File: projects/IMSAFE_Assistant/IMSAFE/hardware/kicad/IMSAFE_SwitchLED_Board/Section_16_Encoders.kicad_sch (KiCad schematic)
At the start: 0 parts

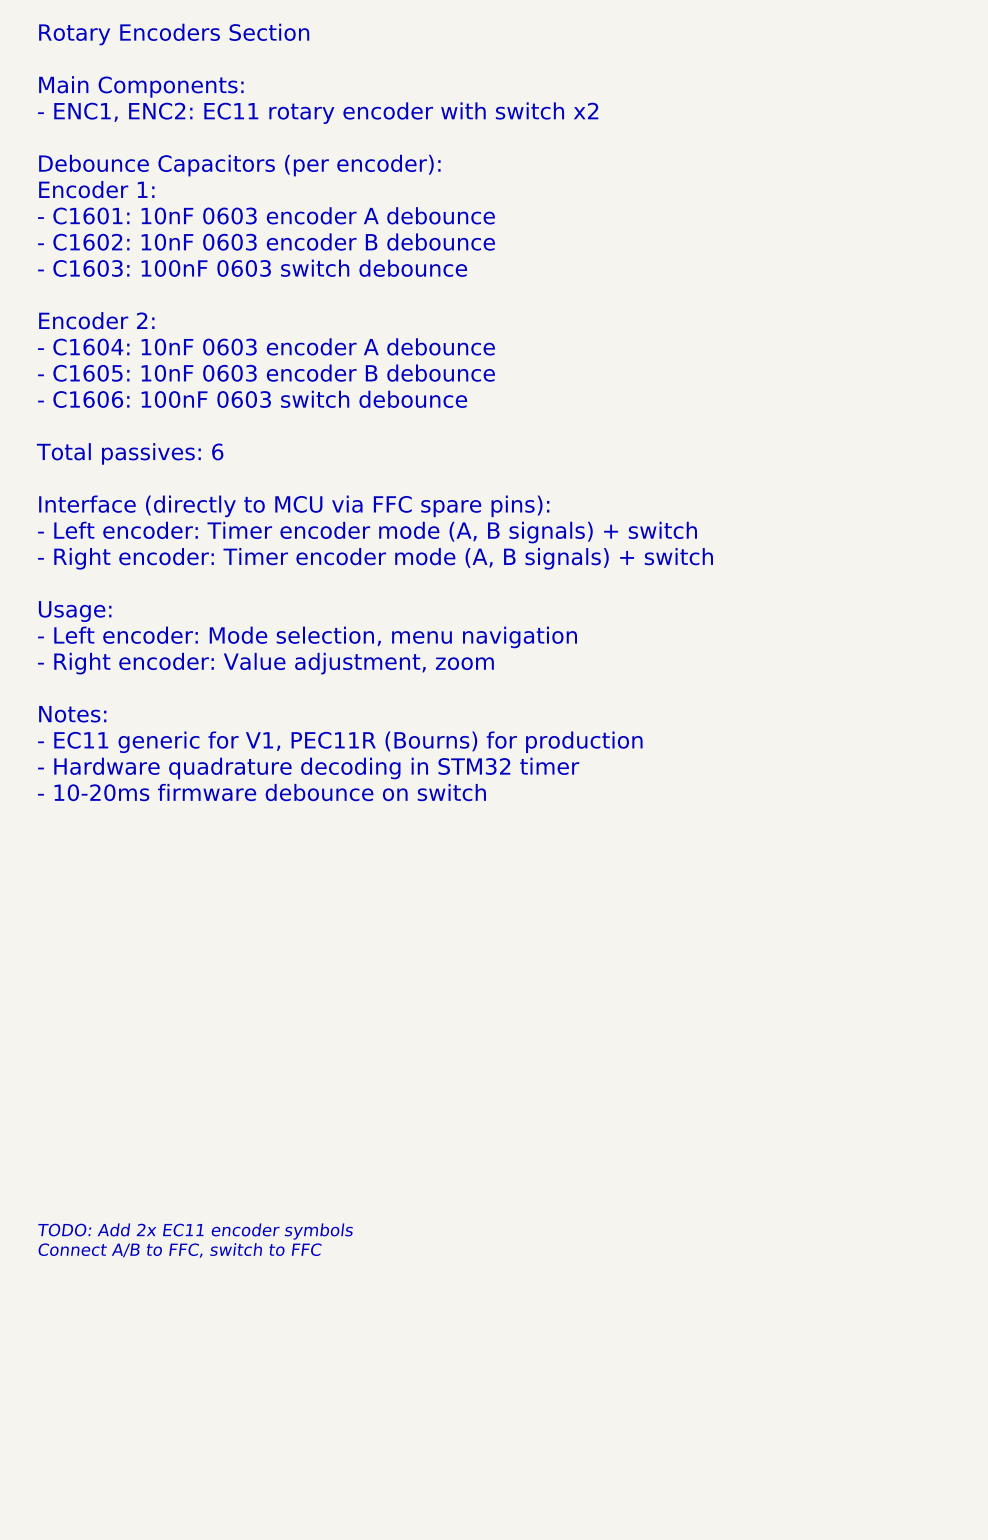
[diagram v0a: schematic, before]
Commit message: Update KiCad schematics and add analysis files
- Update all MainBoard schematic sections with component placement
- Add ERC reports and analysis scripts for schematic validation
- Update Radar Interface and SwitchLED Board projects
- Sync KiCad project files with latest session changes

Co-Authored-By: Claude Opus 4.5 <noreply@anthropic.com>
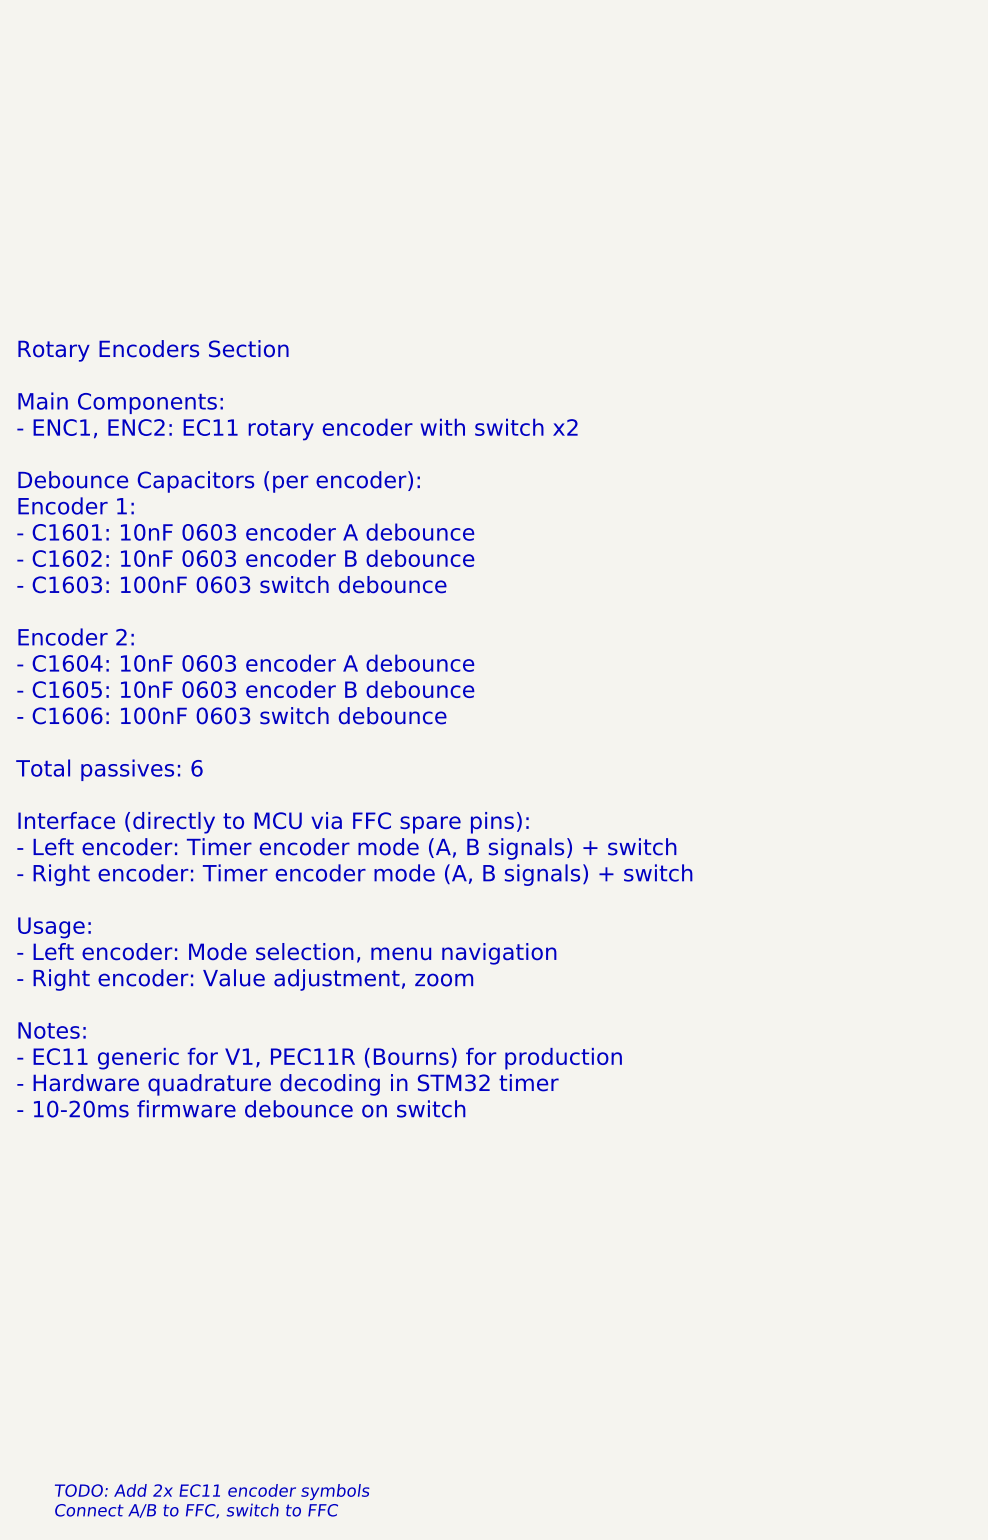
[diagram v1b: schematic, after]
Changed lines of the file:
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@@
 (kicad_sch
-	(version 20231120)
+	(version 20250114)
 	(generator "eeschema")
-	(generator_version "8.0")
-	(uuid "sec16-0001-0002-0003-000000000001")
+	(generator_version "9.0")
 	(paper "A4")
 	(title_block
@@
 		(comment 2 "Menu navigation and value adjustment")
 	)
-	(text "Rotary Encoders Section\n\nMain Components:\n- ENC1, ENC2: EC11 rotary encoder with switch x2\n\nDebounce Capacitors (per encoder):\nEncoder 1:\n- C1601: 10nF 0603 encoder A debounce\n- C1602: 10nF 0603 encoder B debounce\n- C1603: 100nF 0603 switch debounce\n\nEncoder 2:\n- C1604: 10nF 0603 encoder A debounce\n- C1605: 10nF 0603 encoder B debounce\n- C1606: 100nF 0603 switch debounce\n\nTotal passives: 6\n\nInterface (directly to MCU via FFC spare pins):\n- Left encoder: Timer encoder mode (A, B signals) + switch\n- Right encoder: Timer encoder mode (A, B signals) + switch\n\nUsage:\n- Left encoder: Mode selection, menu navigation\n- Right encoder: Value adjustment, zoom\n\nNotes:\n- EC11 generic for V1, PEC11R (Bourns) for production\n- Hardware quadrature decoding in STM32 timer\n- 10-20ms firmware debounce on switch"
-		(exclude_from_sim no)
-		(at 25.4 25.4 0)
-		(effects
-			(font
-				(size 2 2)
-			)
-			(justify left)
-		)
-		(uuid "sec16-text-001")
-	)
 	(text "TODO: Add 2x EC11 encoder symbols\nConnect A/B to FFC, switch to FFC"
 		(exclude_from_sim no)
-		(at 25.4 127 0)
+		(at 27.432 159.004 0)
 		(effects
 			(font
@@
 			(justify left)
 		)
-		(uuid "sec16-todo-001")
+	)
+	(text "Rotary Encoders Section\n\nMain Components:\n- ENC1, ENC2: EC11 rotary encoder with switch x2\n\nDebounce Capacitors (per encoder):\nEncoder 1:\n- C1601: 10nF 0603 encoder A debounce\n- C1602: 10nF 0603 encoder B debounce\n- C1603: 100nF 0603 switch debounce\n\nEncoder 2:\n- C1604: 10nF 0603 encoder A debounce\n- C1605: 10nF 0603 encoder B debounce\n- C1606: 100nF 0603 switch debounce\n\nTotal passives: 6\n\nInterface (directly to MCU via FFC spare pins):\n- Left encoder: Timer encoder mode (A, B signals) + switch\n- Right encoder: Timer encoder mode (A, B signals) + switch\n\nUsage:\n- Left encoder: Mode selection, menu navigation\n- Right encoder: Value adjustment, zoom\n\nNotes:\n- EC11 generic for V1, PEC11R (Bourns) for production\n- Hardware quadrature decoding in STM32 timer\n- 10-20ms firmware debounce on switch"
+		(exclude_from_sim no)
+		(at 22.86 64.262 0)
+		(effects
+			(font
+				(size 2 2)
+			)
+			(justify left)
+		)
 	)
 )
